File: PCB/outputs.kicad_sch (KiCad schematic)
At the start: 5 parts, among them J2 OUT_WIN, J5 OUT_DOOR, J6 UART, J7 SPI, J8 CAN

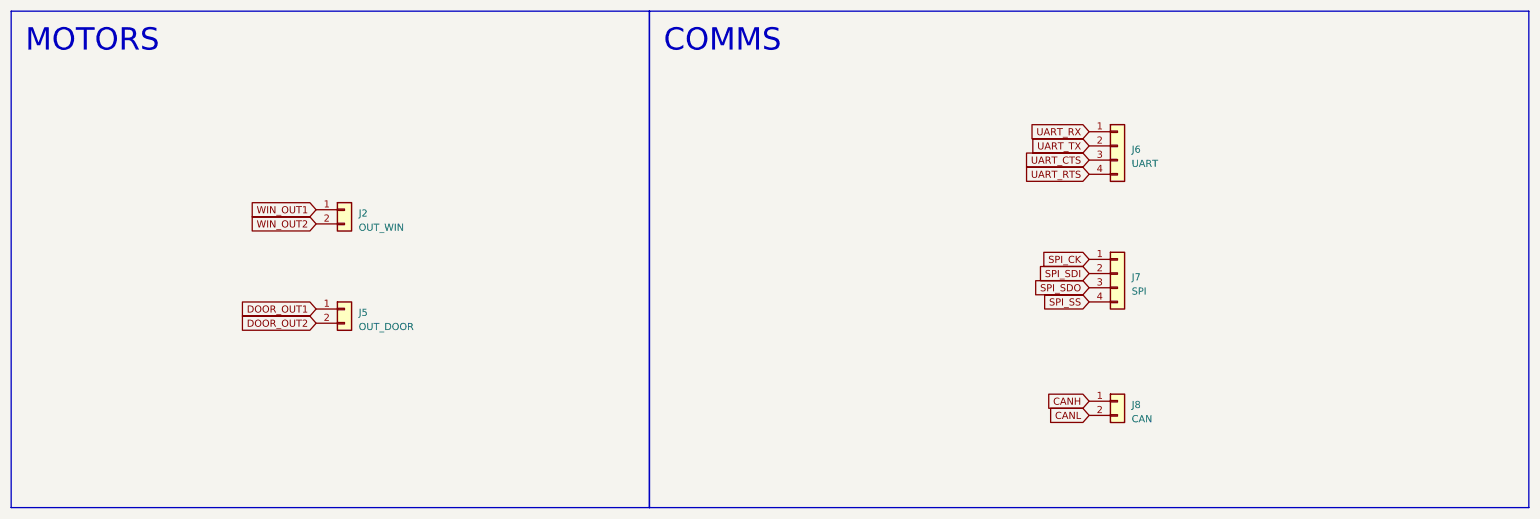
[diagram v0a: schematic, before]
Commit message: correct schematic + README
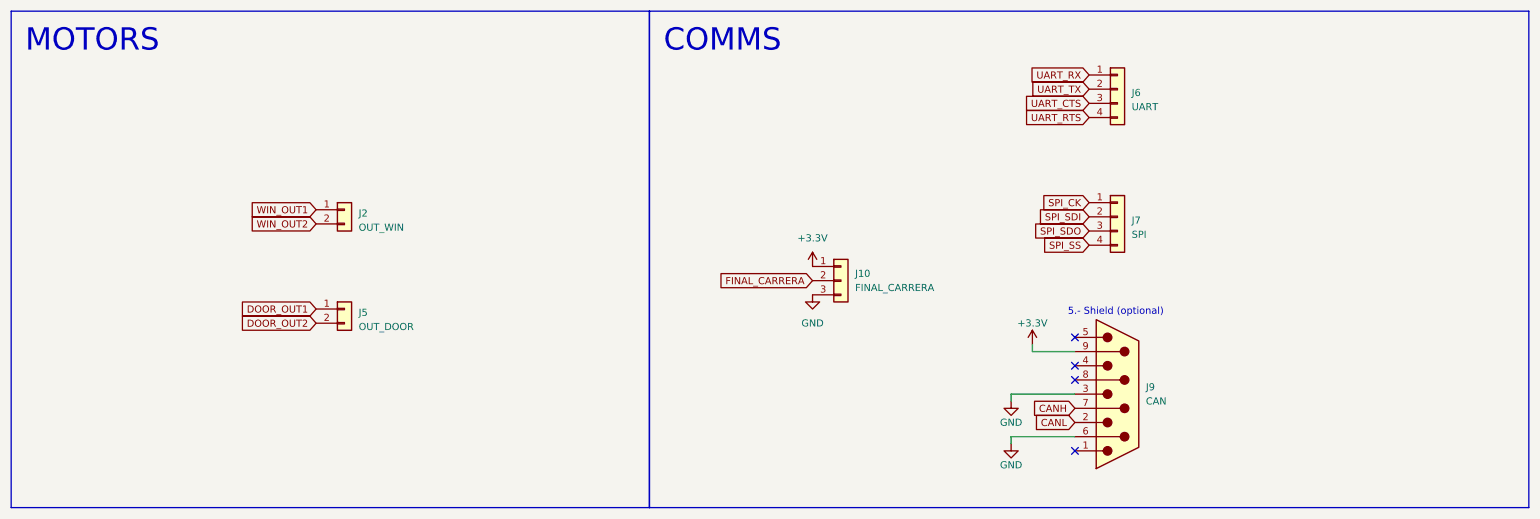
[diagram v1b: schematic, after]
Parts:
- removed J8: CAN, symbol Connector_Generic:Conn_01x02
- added J10: FINAL_CARRERA, symbol Connector_Generic:Conn_01x03
- added J9: CAN, symbol Connector:DE9_Plug
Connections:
- net CANH: now also J9.7
- net CANL: now also J9.2
- new net +3.3V: J10.1 (Pin_1), J9.9
- new net FINAL_CARRERA: J10.2 (Pin_2)
- new net GND: J10.3 (Pin_3), J9.3, J9.6
- no-connect marks 0 -> 4
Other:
- note added: "5.- Shield (optional)"
- moved on the sheet: J6, J7

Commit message: add button controls
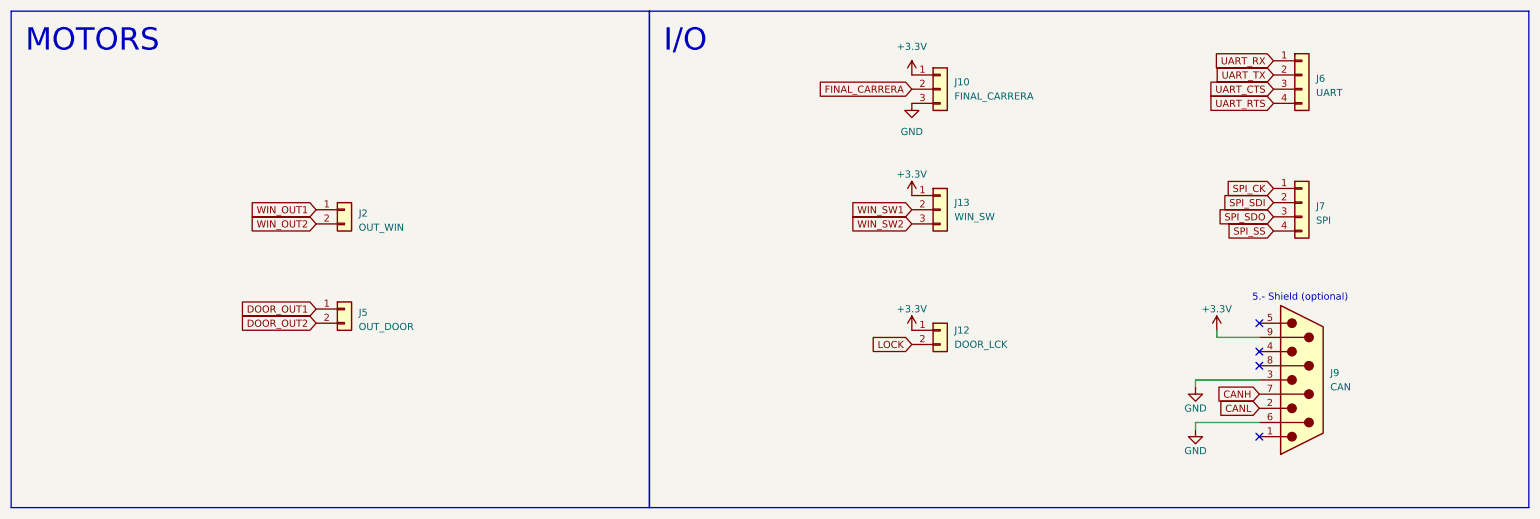
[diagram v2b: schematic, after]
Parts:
- added J12: DOOR_LCK, symbol Connector_Generic:Conn_01x02
- added J13: WIN_SW, symbol Connector_Generic:Conn_01x03
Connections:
- net +3.3V: now also J12.1 (Pin_1), J13.1 (Pin_1)
- new net LOCK: J12.2 (Pin_2)
- new net WIN_SW1: J13.2 (Pin_2)
- new net WIN_SW2: J13.3 (Pin_3)
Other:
- note added: "I/O"
- note removed: "COMMS"
- moved on the sheet: J10, J6, J7, J9

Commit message: sparse changes
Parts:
- removed J6: UART, symbol Connector_Generic:Conn_01x04
- added J11: USART, symbol Connector:DE9_Plug
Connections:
- net GND: now also J11.5
- net UART_RX: now also J11.2
- net UART_TX: now also J11.3
- new net UART_CLK: J11.7
- new net /UART_CTS: J11.8
- no-connect marks 4 -> 8
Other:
- moved on the sheet: J10, J12, J13, J7, J9

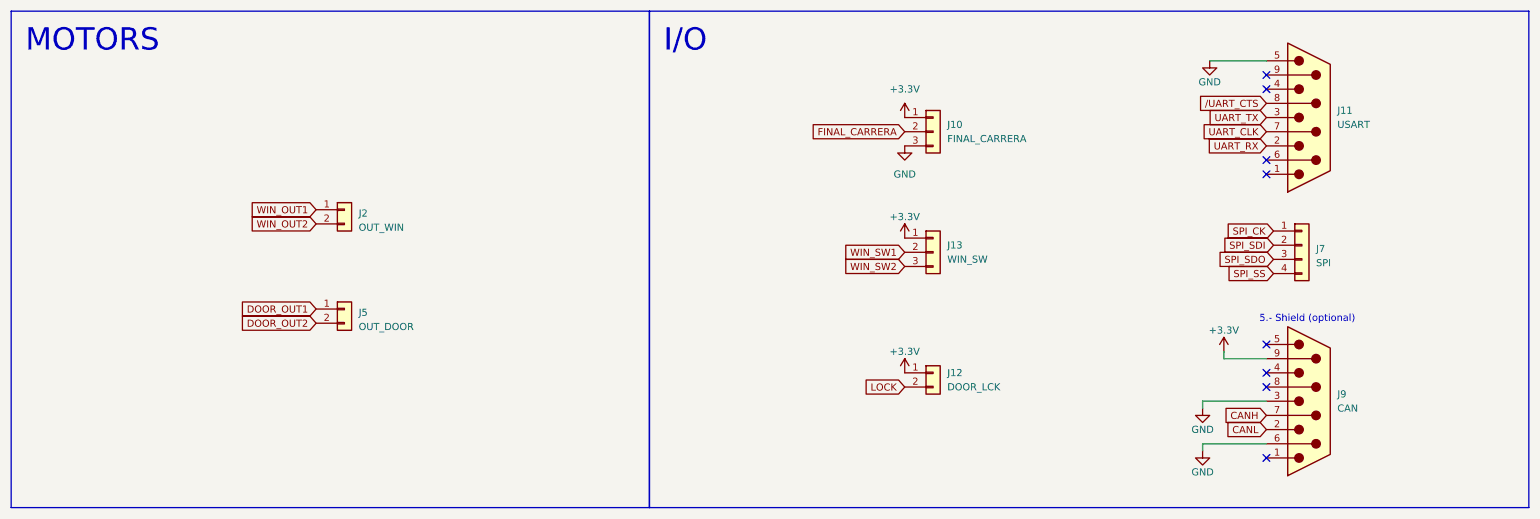
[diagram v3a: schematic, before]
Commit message: change file structure
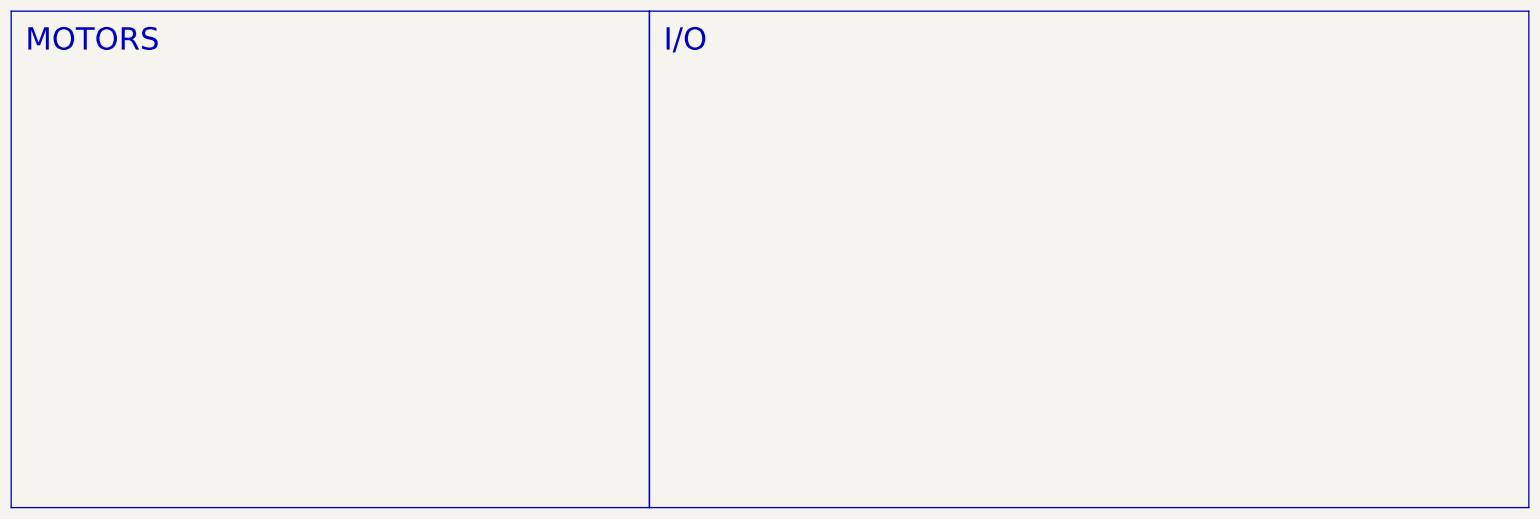
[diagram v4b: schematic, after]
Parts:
- removed J10: FINAL_CARRERA, symbol Connector_Generic:Conn_01x03
- removed J11: USART, symbol Connector:DE9_Plug
- removed J12: DOOR_LCK, symbol Connector_Generic:Conn_01x02
- removed J13: WIN_SW, symbol Connector_Generic:Conn_01x03
- removed J2: OUT_WIN, symbol Connector_Generic:Conn_01x02
- removed J5: OUT_DOOR, symbol Connector_Generic:Conn_01x02
- removed J7: SPI, symbol Connector_Generic:Conn_01x04
- removed J9: CAN, symbol Connector:DE9_Plug
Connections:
- no-connect marks 8 -> 0
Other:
- note removed: "5.- Shield (optional)"
